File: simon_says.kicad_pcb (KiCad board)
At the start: 2 copper layers, 14 parts, among them SW1 SW_Push_LED, SW2 SW_Push_LED, SW3 SW_Push_LED, SW4 SW_Push_LED, U1 ATtiny25-20P

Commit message: First take on component placement
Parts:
- D1, D2, D3, D4: footprint Diode_THT:D_DO-41_SOD81_P10.16mm_Horizontal -> Diode_THT:D_DO-34_SOD68_P7.62mm_Horizontal
- moved SW3 118.5 mm to (132.0, 145.0)
- moved D3 117.9 mm to (122.0, 148.7), turned to 90 degrees
- moved SW2 108.5 mm to (65.0, 145.0)
- moved D6 105.8 mm to (92.5, 155.7), turned to 90 degrees
- moved D8 103.0 mm to (98.5, 155.7), turned to 90 degrees
- moved D10 100.6 mm to (104.5, 155.7), turned to 90 degrees
- moved R1 94.7 mm to (107.3, 147.6), turned to 90 degrees
- moved D2 92.6 mm to (75.0, 141.1), turned to -90 degrees
- moved R2 89.9 mm to (89.7, 147.6), turned to 90 degrees
- moved D4 89.2 mm to (122.0, 111.1), turned to -90 degrees
- moved U1 88.8 mm to (94.7, 140.0)
- moved SW4 85.0 mm to (132.0, 115.0)
- moved SW1 79.2 mm to (65.0, 115.0)
- moved D1 75.4 mm to (75.0, 118.7), turned to 90 degrees
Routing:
- net MM2: track 0.00 -> 75.9 mm
- net Net-(SW1-A): track 0.00 -> 65.4 mm
- net MM3: track 0.00 -> 44.6 mm
- net Net-(D1-A): track 0.00 -> 16.9 mm
- net Net-(D3-A): track 0.00 -> 16.9 mm
- net Net-(D2-A): track 0.00 -> 16.8 mm
- net Net-(D4-A): track 0.00 -> 16.8 mm
- net MM1: track 0.00 -> 12.7 mm
- net MM4: track 0.00 -> 12.7 mm
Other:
- board outline added: 97 x 60 mm

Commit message: Finilized routing
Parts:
- moved D4 7.63 mm to (122.0, 118.7), turned to 90 degrees
- moved D3 7.62 mm to (122.0, 141.1), turned to -90 degrees
- moved D6 6.20 mm to (98.5, 154.2), turned to -90 degrees
- moved D8 6.20 mm to (92.5, 154.2), turned to -90 degrees
- moved R2 5.59 mm to (89.7, 142.0), turned to -90 degrees
- moved R1 2.03 mm to (107.3, 149.6)
- moved U1 2.00 mm to (94.7, 142.0)
- moved D10 1.55 mm to (104.5, 154.2), turned to -90 degrees
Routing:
- net BTNS: track 0.00 -> 100.0 mm
- net Net-(SW1-A): track 65.4 -> 147.3 mm
- net MM1: track 12.7 -> 82.5 mm
- net MM4: track 12.7 -> 80.1 mm
- net MM2: track 75.9 -> 124.2 mm
- net MM3: track 44.6 -> 81.0 mm
- net Net-(D10-A): track 0.00 -> 21.0 mm
- net Net-(D4-A): track 16.8 -> 20.9 mm
- net Net-(D3-A): track 16.9 -> 20.6 mm
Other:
- board size 97 x 60 mm -> 138.4 x 60 mm

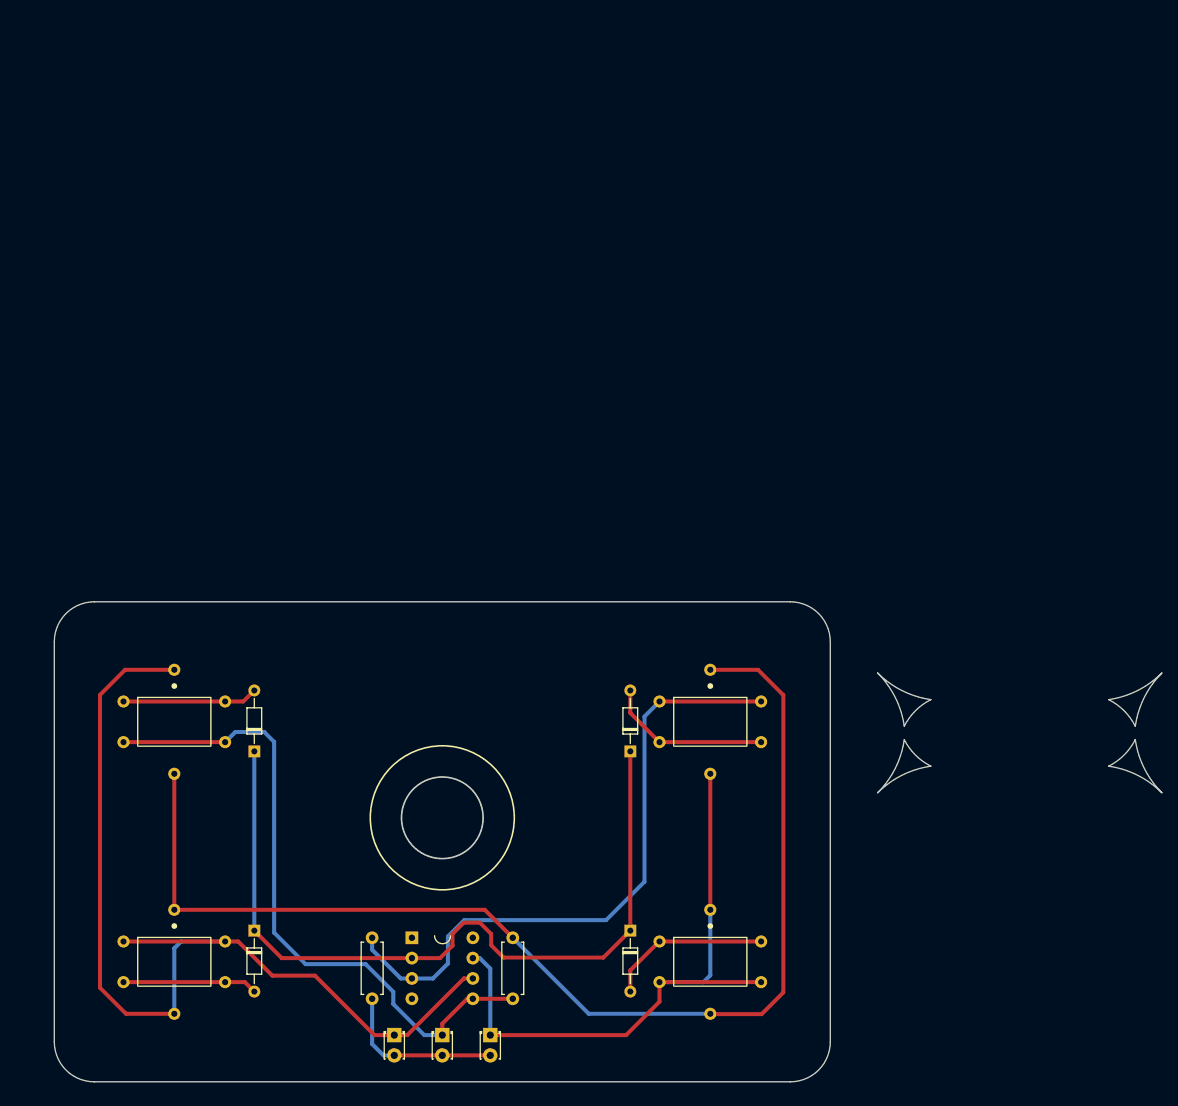
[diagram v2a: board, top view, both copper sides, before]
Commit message: Added cutouts and decorations
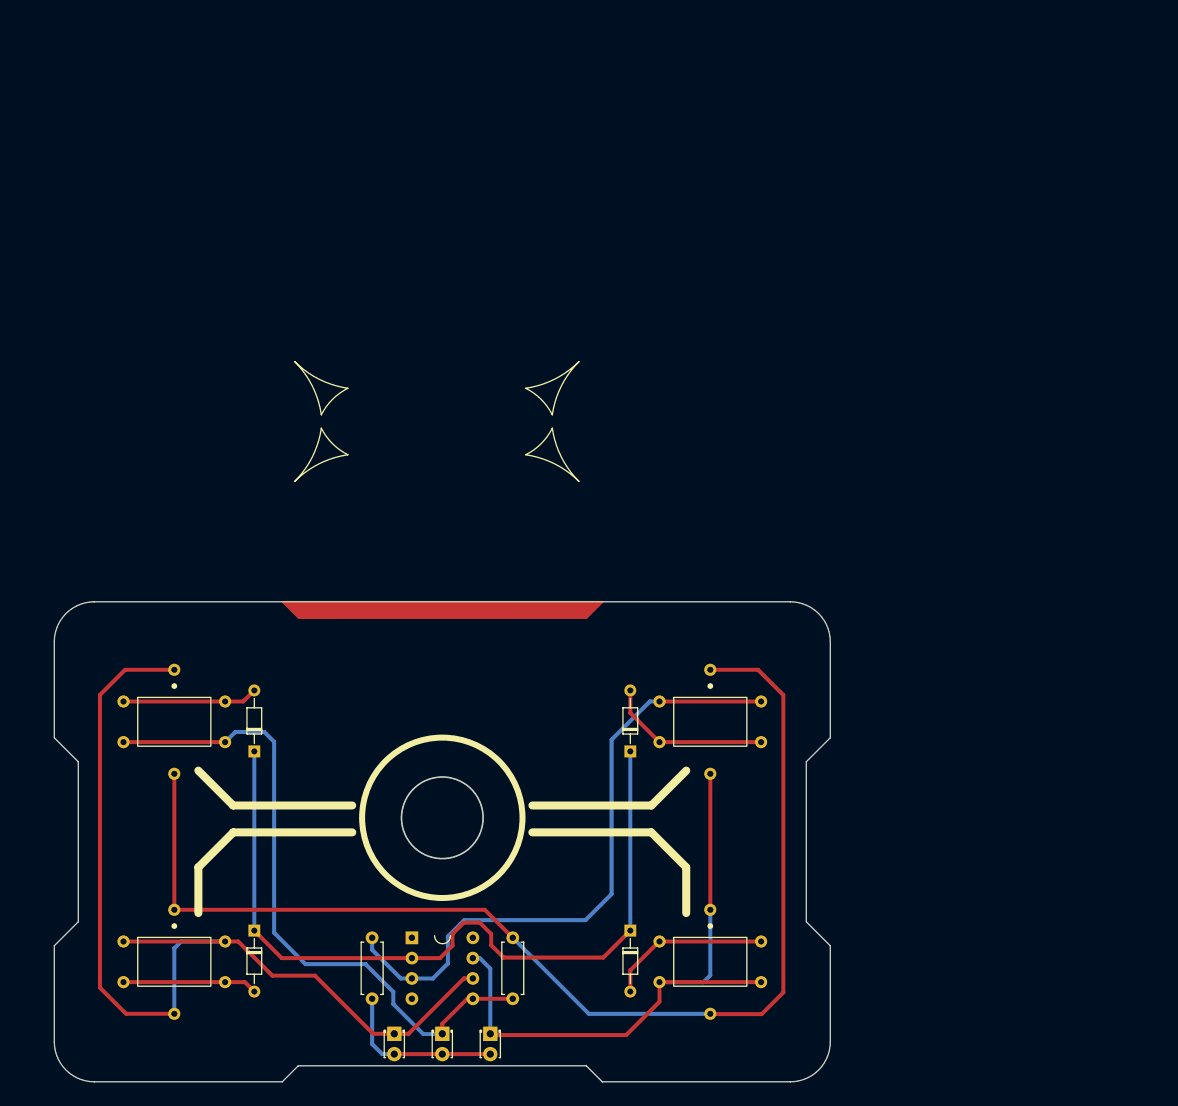
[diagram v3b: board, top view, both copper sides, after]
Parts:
- moved D10 0.16 mm to (104.5, 154.0)
- moved D6 0.16 mm to (98.5, 154.0)
- moved D8 0.16 mm to (92.5, 154.0)
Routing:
- net MM4: track 80.1 -> 79.3 mm
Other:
- board size 138.4 x 60 mm -> 97 x 60 mm

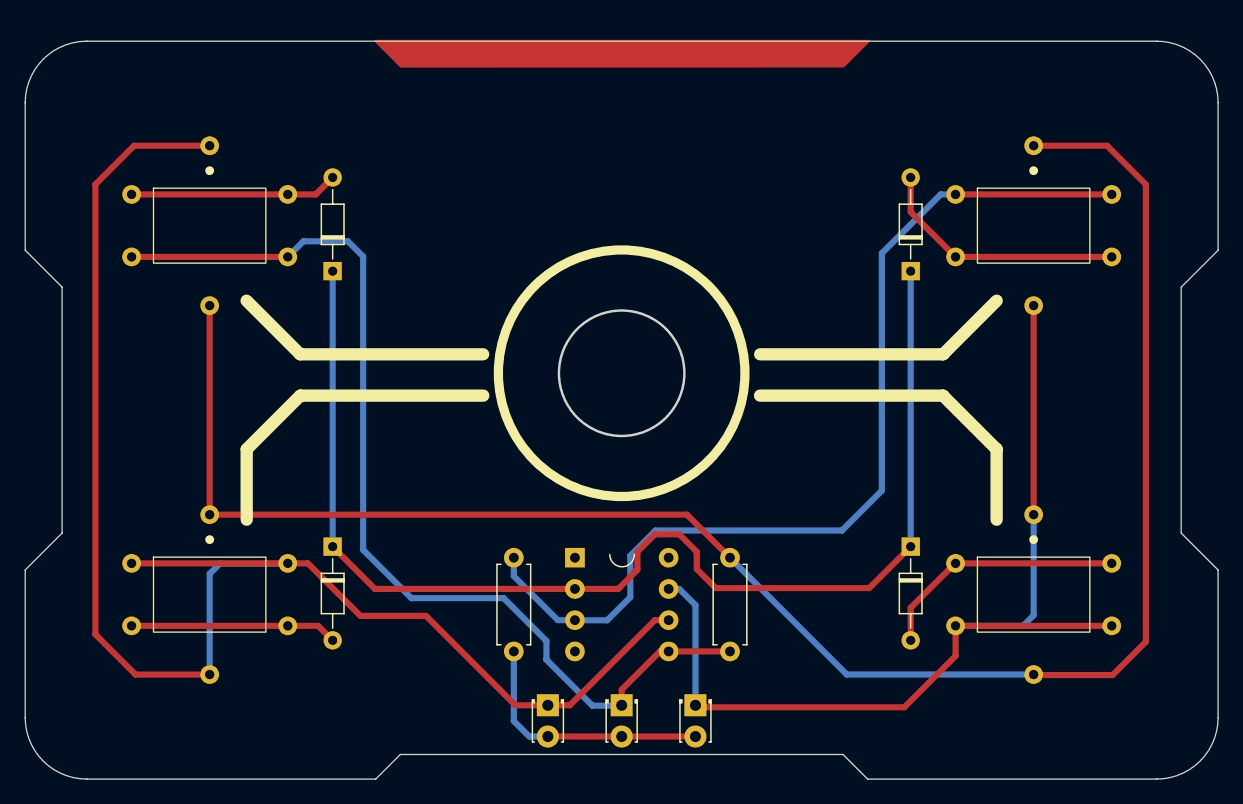
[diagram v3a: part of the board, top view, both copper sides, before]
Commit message: Added mounting holes
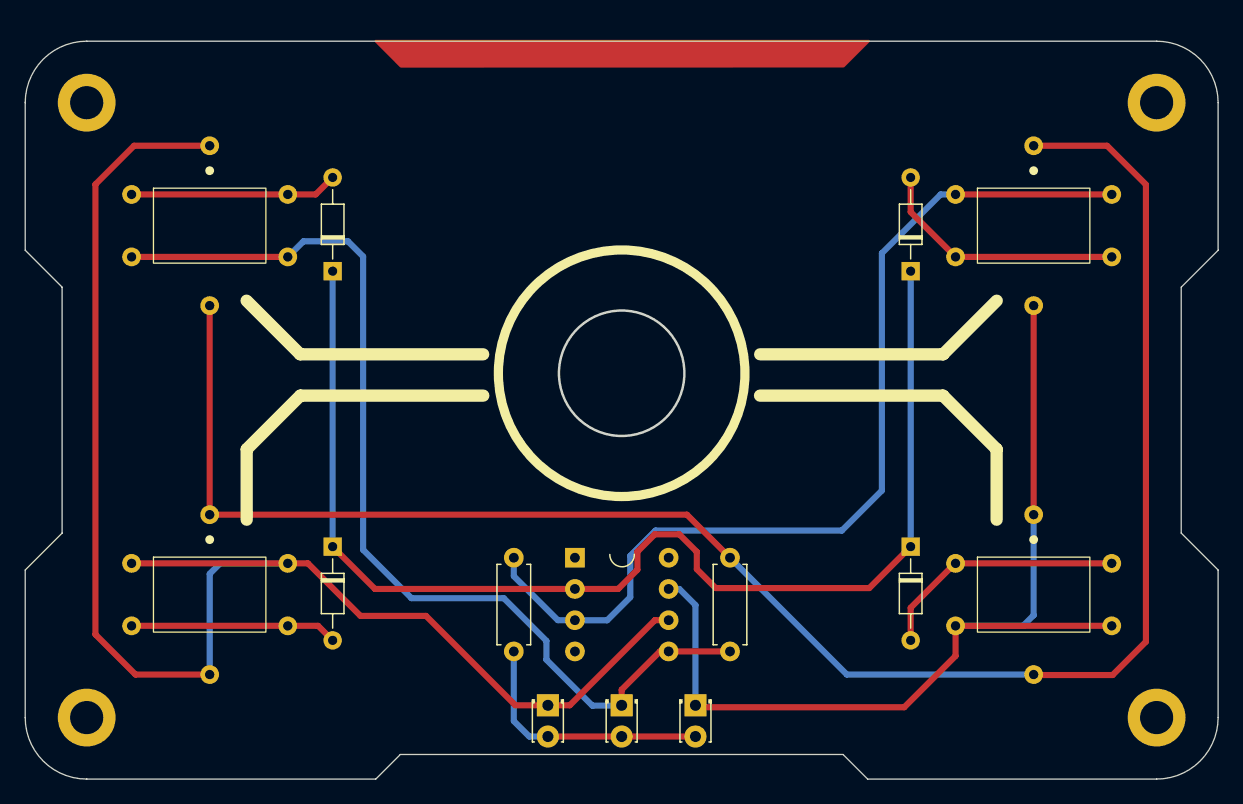
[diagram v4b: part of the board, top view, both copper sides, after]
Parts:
- added REF**: MountingHole_2.7mm_M2.5_DIN965_Pad, MountingHole:MountingHole_2.7mm_M2.5_DIN965_Pad, F.Cu at (55.0, 105.0)
- added REF**: MountingHole_2.7mm_M2.5_DIN965_Pad, MountingHole:MountingHole_2.7mm_M2.5_DIN965_Pad, F.Cu at (142.0, 155.0)
- added REF**: MountingHole_2.7mm_M2.5_DIN965_Pad, MountingHole:MountingHole_2.7mm_M2.5_DIN965_Pad, F.Cu at (142.0, 105.0)
- added REF**: MountingHole_2.7mm_M2.5_DIN965_Pad, MountingHole:MountingHole_2.7mm_M2.5_DIN965_Pad, F.Cu at (55.0, 155.0)
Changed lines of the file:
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@@
     )
+  )
+  (footprint "MountingHole:MountingHole_2.7mm_M2.5_DIN965_Pad" (layer "F.Cu")
+    (at 55 105)
+    (descr "Mounting Hole 2.7mm, M2.5, DIN965")
+    (tags "mounting hole 2.7mm m2.5 din965")
+    (attr exclude_from_pos_files exclude_from_bom)
+    (fp_text reference "REF**" (at 0 -3.35) (layer "F.SilkS") hide
+        (effects (font (size 1 1) (thickness 0.15)))
+    )
+    (fp_text value "MountingHole_2.7mm_M2.5_DIN965_Pad" (at 0 3.35) (layer "F.Fab") hide
+        (effects (font (size 1 1) (thickness 0.15)))
+    )
+    (fp_text user "${REFERENCE}" (at 0 0) (layer "F.Fab") hide
+        (effects (font (size 1 1) (thickness 0.15)))
+    )
+    (fp_circle (center 0 0) (end 2.35 0)
+      (stroke (width 0.15) (type solid)) (fill none) (layer "Cmts.User"))
+    (fp_circle (center 0 0) (end 2.6 0)
+      (stroke (width 0.05) (type solid)) (fill none) (layer "F.CrtYd"))
+    (pad "1" thru_hole circle (at 0 0) (size 4.7 4.7) (drill 2.7) (layers "*.Cu" "*.Mask"))
   )
   (footprint "Diode_THT:D_DO-34_SOD68_P7.62mm_Horizontal" (layer "F.Cu")
@@
     )
   )
+  (footprint "MountingHole:MountingHole_2.7mm_M2.5_DIN965_Pad" (layer "F.Cu")
+    (at 142 155)
+    (descr "Mounting Hole 2.7mm, M2.5, DIN965")
+    (tags "mounting hole 2.7mm m2.5 din965")
+    (attr exclude_from_pos_files exclude_from_bom)
+    (fp_text reference "REF**" (at 0 -3.35) (layer "F.SilkS") hide
+        (effects (font (size 1 1) (thickness 0.15)))
+    )
+    (fp_text value "MountingHole_2.7mm_M2.5_DIN965_Pad" (at 0 3.35) (layer "F.Fab") hide
+        (effects (font (size 1 1) (thickness 0.15)))
+    )
+    (fp_text user "${REFERENCE}" (at 0 0) (layer "F.Fab") hide
+        (effects (font (size 1 1) (thickness 0.15)))
+    )
+    (fp_circle (center 0 0) (end 2.35 0)
+      (stroke (width 0.15) (type solid)) (fill none) (layer "Cmts.User"))
+    (fp_circle (center 0 0) (end 2.6 0)
+      (stroke (width 0.05) (type solid)) (fill none) (layer "F.CrtYd"))
+    (pad "1" thru_hole circle (at 0 0) (size 4.7 4.7) (drill 2.7) (layers "*.Cu" "*.Mask"))
+  )
+  (footprint "MountingHole:MountingHole_2.7mm_M2.5_DIN965_Pad" (layer "F.Cu")
+    (at 142 105)
+    (descr "Mounting Hole 2.7mm, M2.5, DIN965")
+    (tags "mounting hole 2.7mm m2.5 din965")
+    (attr exclude_from_pos_files exclude_from_bom)
+    (fp_text reference "REF**" (at 0 -3.35) (layer "F.SilkS") hide
+        (effects (font (size 1 1) (thickness 0.15)))
+    )
+    (fp_text value "MountingHole_2.7mm_M2.5_DIN965_Pad" (at 0 3.35) (layer "F.Fab") hide
+        (effects (font (size 1 1) (thickness 0.15)))
+    )
+    (fp_text user "${REFERENCE}" (at 0 0) (layer "F.Fab") hide
+        (effects (font (size 1 1) (thickness 0.15)))
+    )
+    (fp_circle (center 0 0) (end 2.35 0)
+      (stroke (width 0.15) (type solid)) (fill none) (layer "Cmts.User"))
+    (fp_circle (center 0 0) (end 2.6 0)
+      (stroke (width 0.05) (type solid)) (fill none) (layer "F.CrtYd"))
+    (pad "1" thru_hole circle (at 0 0) (size 4.7 4.7) (drill 2.7) (layers "*.Cu" "*.Mask"))
+  )
   (footprint "LED_THT:LED_D1.8mm_W3.3mm_H2.4mm" (layer "F.Cu")
     (at 104.5 154 -90)
@@
     )
   )
+  (footprint "MountingHole:MountingHole_2.7mm_M2.5_DIN965_Pad" (layer "F.Cu")
+    (at 55 155)
+    (descr "Mounting Hole 2.7mm, M2.5, DIN965")
+    (tags "mounting hole 2.7mm m2.5 din965")
+    (attr exclude_from_pos_files exclude_from_bom)
+    (fp_text reference "REF**" (at 0 -3.35) (layer "F.SilkS") hide
+        (effects (font (size 1 1) (thickness 0.15)))
+    )
+    (fp_text value "MountingHole_2.7mm_M2.5_DIN965_Pad" (at 0 3.35) (layer "F.Fab") hide
+        (effects (font (size 1 1) (thickness 0.15)))
+    )
+    (fp_text user "${REFERENCE}" (at 0 0) (layer "F.Fab") hide
+        (effects (font (size 1 1) (thickness 0.15)))
+    )
+    (fp_circle (center 0 0) (end 2.35 0)
+      (stroke (width 0.15) (type solid)) (fill none) (layer "Cmts.User"))
+    (fp_circle (center 0 0) (end 2.6 0)
+      (stroke (width 0.05) (type solid)) (fill none) (layer "F.CrtYd"))
+    (pad "1" thru_hole circle (at 0 0) (size 4.7 4.7) (drill 2.7) (layers "*.Cu" "*.Mask"))
+  )
   (gr_poly

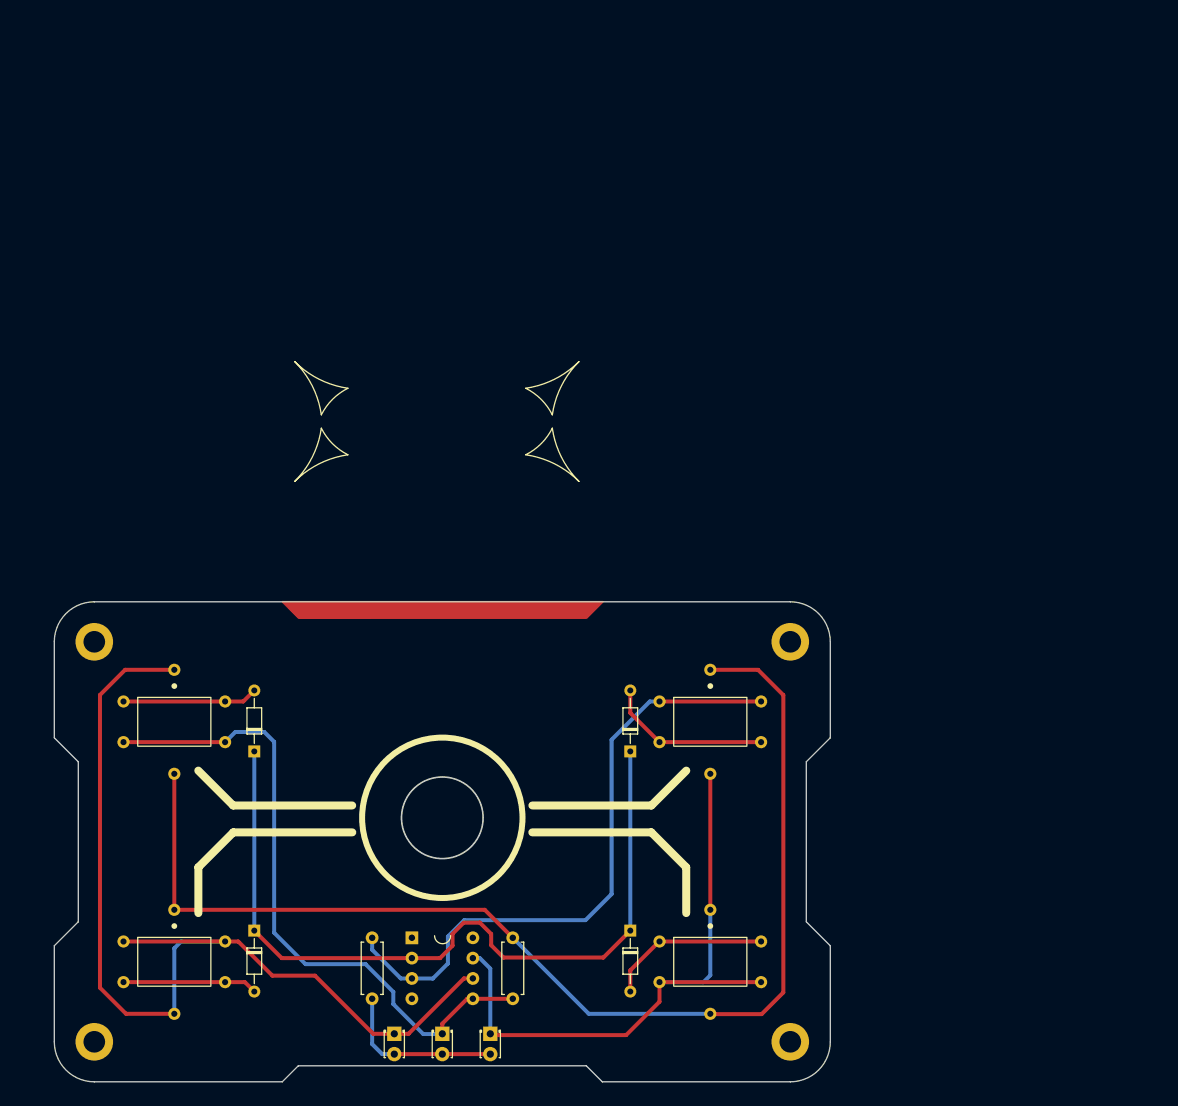
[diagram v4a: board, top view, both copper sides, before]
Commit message: Added speaker
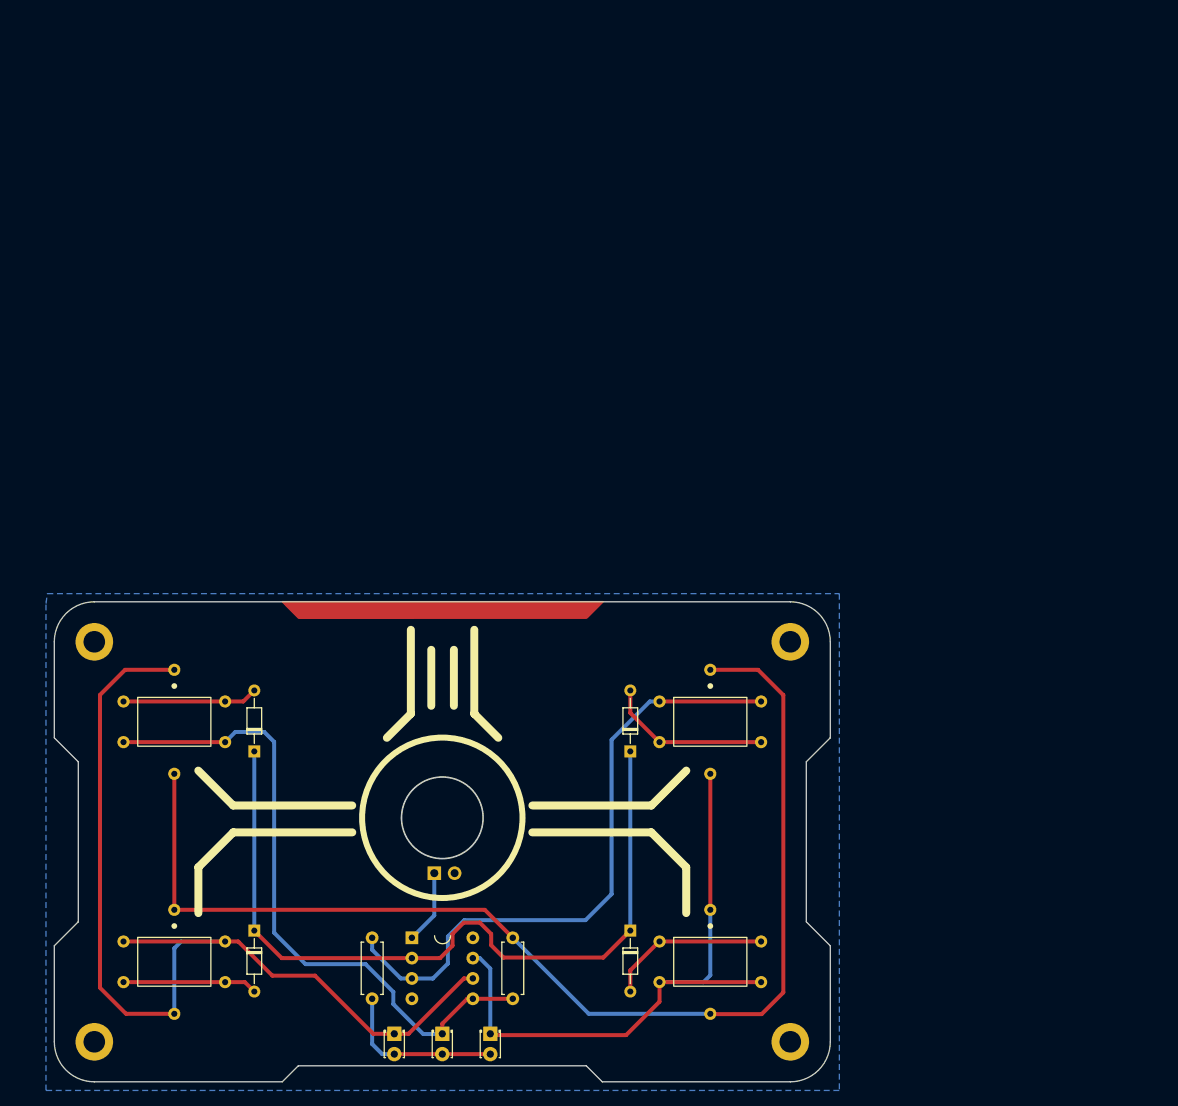
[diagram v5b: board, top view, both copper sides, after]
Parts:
- added LS1: Speaker, Connector_PinHeader_2.54mm:PinHeader_1x02_P2.54mm_Vertical, F.Cu at (97.5, 133.9)
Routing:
- net SPK: track 0.00 -> 9.24 mm
- added copper zone on B.Cu, net -BATT

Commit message: Applied aesthetic modifications
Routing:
- net BTNS: track 100.0 -> 107.2 mm
- net MM2: track 124.0 -> 125.9 mm
